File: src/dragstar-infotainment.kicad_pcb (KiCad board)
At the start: 2 copper layers, 75 x 100 mm, 71 parts, among them J10 Conn_01x01, J11 Conn_01x01, J12 Conn_01x01, J13 Conn_01x01, J14 Conn_01x01, J15 Conn_01x01, J16 Conn_01x01, J17 Conn_01x01, J18 Conn_01x01, J19 Conn_01x01, J20 Conn_01x01, J21 Conn_01x01, J22 Conn_01x01, J23 XT60-M, J24 Conn_01x01, J25 Conn_01x01, J26 1217080-1, J27 1217080-1, J28 1217080-1, J29 1217080-1, J3 Conn_01x01, J30 1217080-1, J31 1217080-1, J32 1217080-1, J33 1217080-1, J34 1217080-1, J35 1217080-1, J4 Conn_01x01, J5 Conn_01x01, J6 Conn_01x01, J7 Conn_01x01, J8 Conn_01x01, J9 Conn_01x01, K1 RAYEX-L90, K2 LEG-12, K3 LEG-12, Q1 2N7002, Q2 2N7002, Q3 2N7002, Q4 2N7002, Q5 2N7002, Q6 2N7002

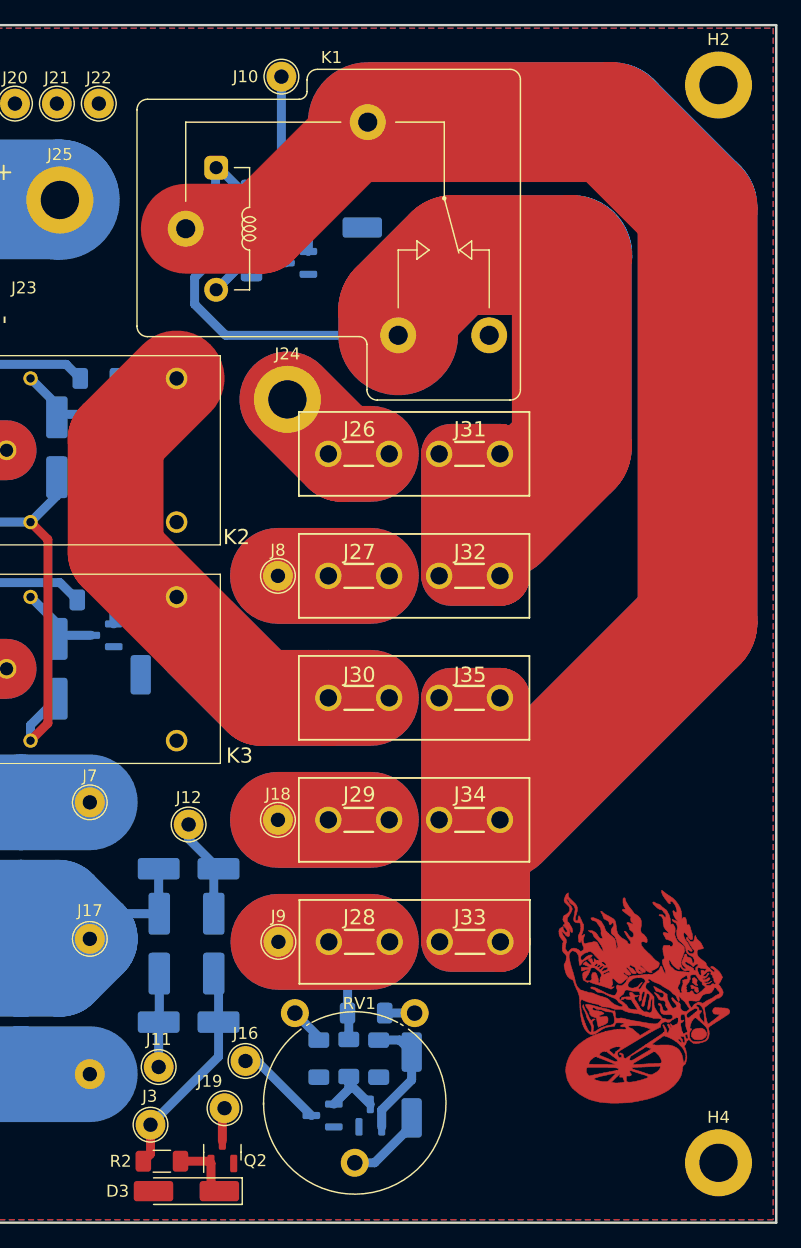
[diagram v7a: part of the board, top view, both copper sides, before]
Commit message: Add LED Blinkers balasts; Update PCB
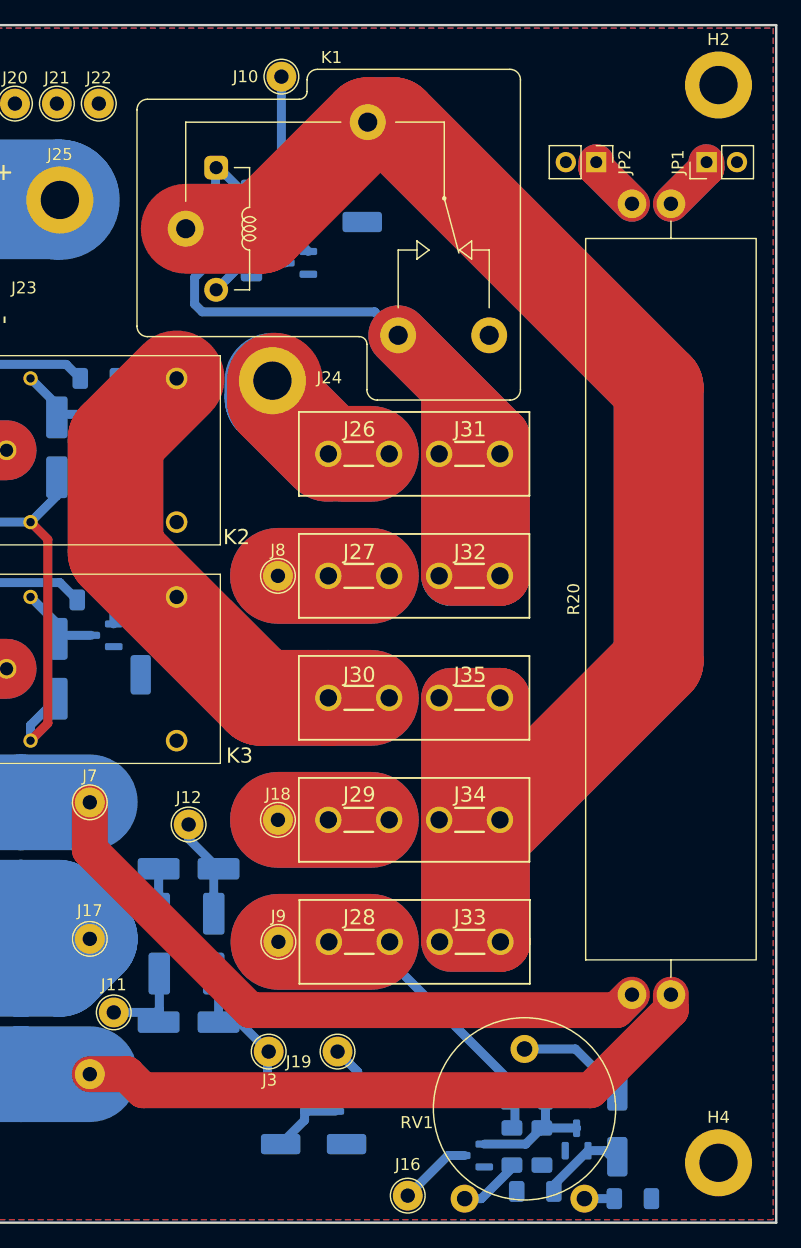
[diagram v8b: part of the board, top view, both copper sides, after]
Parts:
- added JP1: Jumper_2_Bridged, Connector_PinHeader_2.54mm:PinHeader_1x02_P2.54mm_Vertical, F.Cu at (173.0, 61.2)
- added JP2: Jumper_2_Bridged, Connector_PinHeader_2.54mm:PinHeader_1x02_P2.54mm_Vertical, F.Cu at (163.8, 61.2)
- added R17: 1.5K, Resistor_SMD:R_1206_3216Metric_Pad1.30x1.75mm_HandSolder, B.Cu at (158.0, 139.5)
- added R20: 15W, Resistor_THT:R_Axial_Power_L60.0mm_W14.0mm_P66.04mm, F.Cu at (170.0, 130.8)
- added R21: 15W, Resistor_THT:R_Axial_Power_L60.0mm_W14.0mm_P66.04mm, B.Cu at (166.8, 130.8)
- D3, Q2, R2: moved to B.Cu
- R3: value 1.5K -> 10K
- R5: value 11K -> 10K
- RV1: value 5K -> 4.7K
- moved R6 28.7 mm to (166.8, 147.8), turned to 180 degrees
- moved RV1 28.7 mm to (162.8, 147.8), turned to 90 degrees
- moved R3 17.7 mm to (159.2, 143.4)
- moved J16 17.6 mm to (148.1, 147.6), turned to 90 degrees
- moved D12 17.5 mm to (165.6, 141.6), turned to -90 degrees
- moved Q4 17.3 mm to (162.2, 142.9)
- moved R5 17.1 mm to (158.7, 147.2), turned to 0 degrees
- moved R4 16.5 mm to (156.8, 143.4), turned to 90 degrees
- moved Q3 13.0 mm to (153.5, 144.2)
- moved R2 11.8 mm to (137.9, 139.0)
- moved J3 11.6 mm to (136.4, 135.5), turned to 0 degrees
- moved D3 11.3 mm to (140.2, 143.2), turned to 0 degrees
- moved Q2 11.3 mm to (142.9, 139.6), turned to 0 degrees
- moved J19 10.6 mm to (142.2, 135.5), turned to 0 degrees
- moved J11 5.90 mm to (123.5, 132.2)
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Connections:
- net /Main board/RelayGnd renamed Net-(D1-A)
- R3 pad 1: Net-(Q3-G) -> GND
- R3 pad 2: VInst -> Net-(Q3-G)
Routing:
- net RBlinker: track 12.5 -> 67.8 mm
- net LBlinker: track 12.5 -> 65.6 mm
- net MainRelay: track 189.0 -> 154.2 mm
- net +12V: track 346.8 -> 320.1 mm
- net VInst: track 24.4 -> 36.1 mm
- net Net-(JP2-A): track 0.00 -> 9.41 mm
- net Net-(JP1-A): track 0.00 -> 9.41 mm
- net PLight: track 18.4 -> 13.0 mm
- net Net-(Q3-G): track 5.89 -> 10.8 mm
- net Net-(D12-A): track 10.4 -> 7.24 mm
- net Killswitch: track 17.7 -> 20.8 mm
- net Net-(R4-Pad1): track 2.50 -> 5.36 mm
- net Net-(D12-K): track 6.69 -> 9.20 mm
- net Net-(D3-K): track 5.23 -> 7.62 mm
- net GNDDash: track 2.81 -> 4.73 mm
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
